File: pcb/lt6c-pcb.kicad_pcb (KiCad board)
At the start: 2 copper layers, 62 x 66.4 mm, 19 parts, among them SW1 SW_Push, SW2 SW_Push, SW3 SW_Push, SW4 SW_Push, SW5 SW_Push, SW6 SW_Push, U1 XIAO-RP2040, U2 TPS76318, U3 PMW3360DM-T2QU

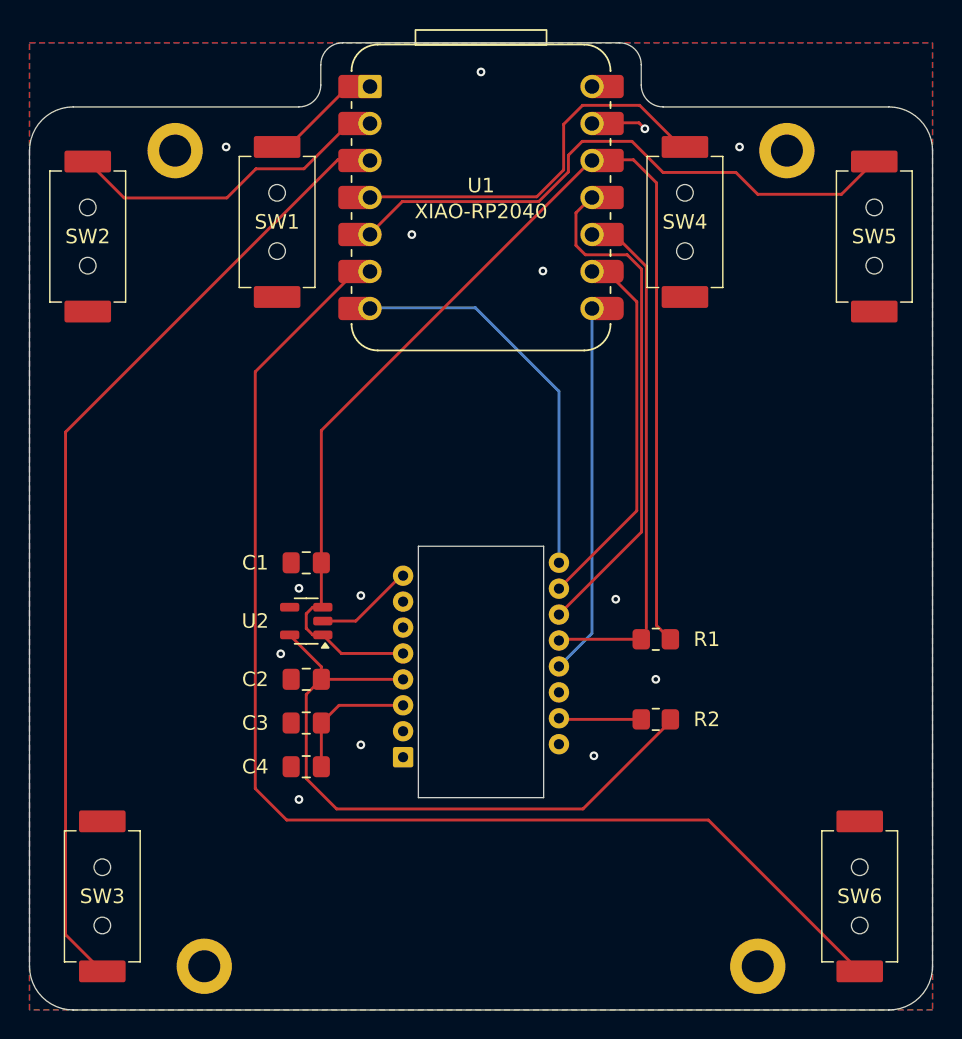
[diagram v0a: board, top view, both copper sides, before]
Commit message: Add silkscreen pattern and infos
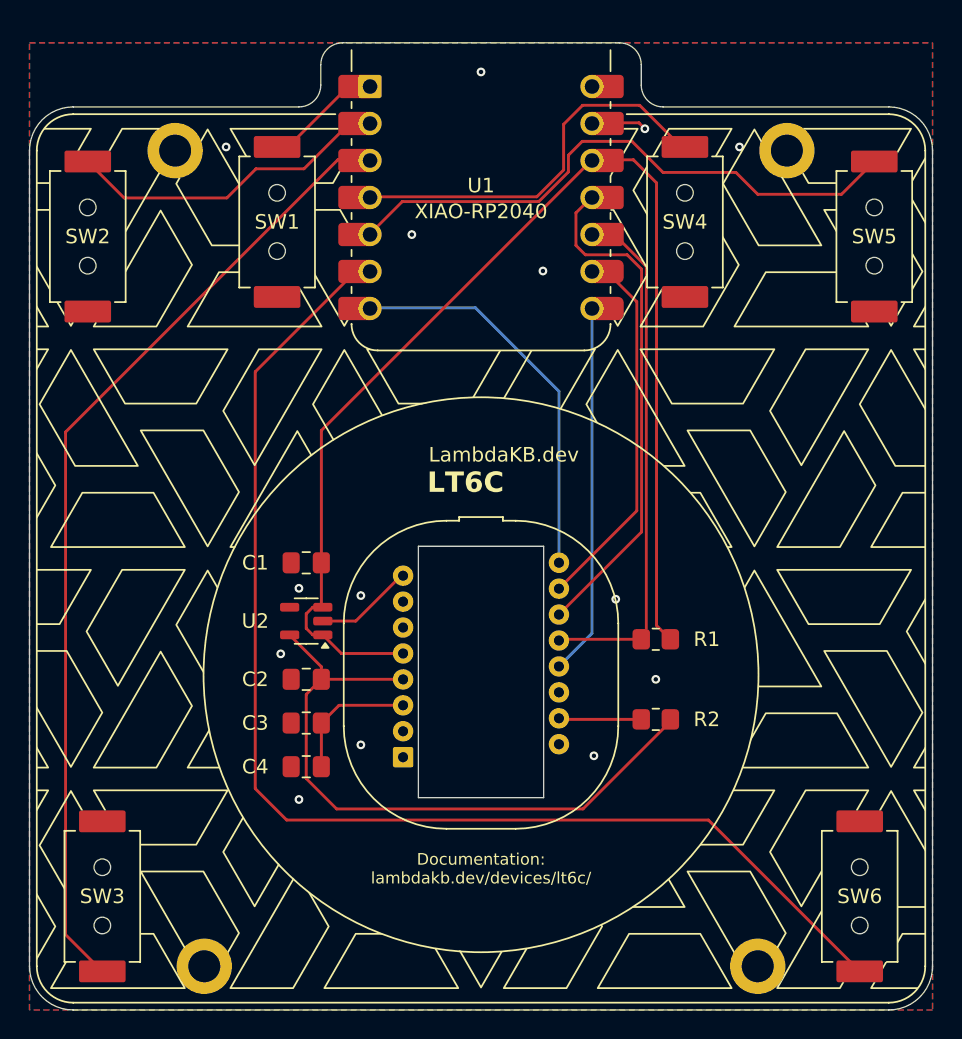
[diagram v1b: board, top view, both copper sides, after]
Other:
- board text added: "2025 - LambdaKB.dev"
- board text added: "CERN-OHL-S-2.0"
- board text added: "Documentation: lambdakb.dev/devices/lt6c/"
- board text added: "LT6C"
- board text added: "LT6C v1.00"
- board text added: "LambdaKB.dev"
- board text added: "PMW3360DM"

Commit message: Update README.md & .gitattributes
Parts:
- H1, H2, H3, H4: value MountingHole_M2 -> MountingHole_Pad
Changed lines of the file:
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@@
 			)
 		)
-		(property "Value" "MountingHole_M2"
+		(property "Value" "MountingHole_Pad"
 			(at 0 2.9 0)
 			(layer "F.Fab")
@@
 			)
 		)
-		(property "Value" "MountingHole_M2"
+		(property "Value" "MountingHole_Pad"
 			(at 0 2.9 0)
 			(layer "F.Fab")
@@
 			)
 		)
-		(property "Value" "MountingHole_M2"
+		(property "Value" "MountingHole_Pad"
 			(at 0 2.9 0)
 			(layer "F.Fab")
@@
 			)
 		)
-		(property "Value" "MountingHole_M2"
+		(property "Value" "MountingHole_Pad"
 			(at 0 2.9 0)
 			(layer "F.Fab")
@@
 			)
 		)
-		(property "Datasheet" ""
+		(property "Datasheet" "https://www.epsglobal.com/Media-Library/EPSGlobal/Products/files/pixart/PMW3360DM-T2QU.pdf"
 			(at 0 0 180)
 			(layer "B.Fab")

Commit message: Update silkscreen
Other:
- board text added: "Licensed under"

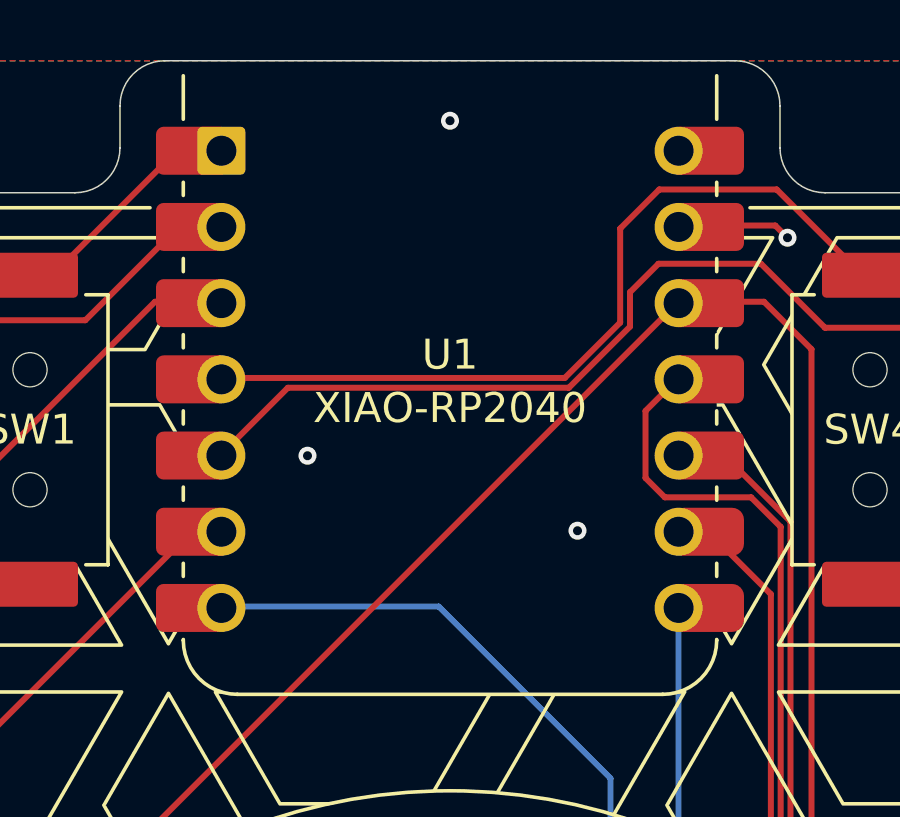
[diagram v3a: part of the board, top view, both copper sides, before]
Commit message: Add pinouts to XIAO-RP2040 and cleanup silkscreen
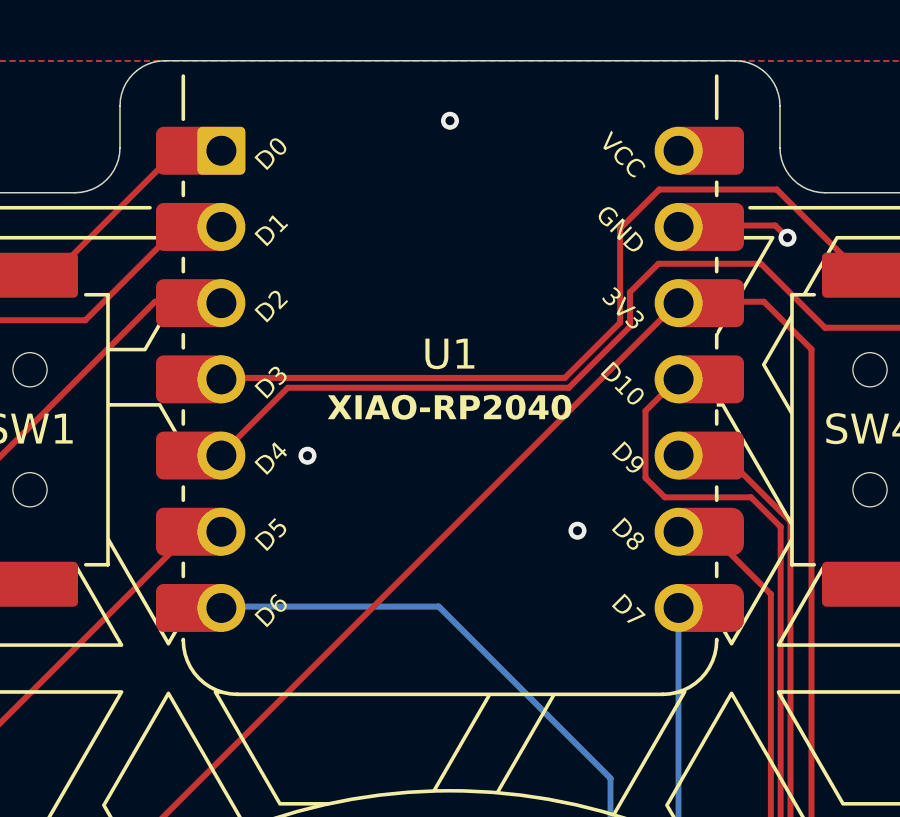
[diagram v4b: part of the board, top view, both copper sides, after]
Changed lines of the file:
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@@
 	(net 27 "unconnected-(U3-NC-Pad14)")
 	(net 28 "unconnected-(U3-NC-Pad6)")
-	(net 29 "unconnected-(U1-5V-Pad14)")
 	(footprint "Capacitor_SMD:C_0805_2012Metric_Pad1.18x1.45mm_HandSolder"
 		(layer "F.Cu")
@@
 			(effects
 				(font
-					(size 1 1)
-					(thickness 0.15)
+					(size 0.8 0.8)
+					(thickness 0.16)
+					(bold yes)
 				)
 			)
@@
 		(fp_line
 			(start -8.89 -1.05)
-			(end -8.89 -2.5)
+			(end -8.89 -2.4892)
 			(stroke
 				(width 0.12)
@@
 		)
 		(fp_line
-			(start 8.89 -1.05)
-			(end 8.89 -2.5)
+			(start 8.89 -2.4892)
+			(end 8.89 -1.08)
 			(stroke
 				(width 0.12)
@@
 			(layer "F.Fab")
 		)
-		(fp_rect
-			(start -4.5 -2.88)
-			(end 4.5 -3.88)
-			(stroke
-				(width 0.12)
-				(type solid)
+		(fp_text user "D8"
+			(at 6.35 13.208 -45)
+			(unlocked yes)
+			(layer "F.SilkS")
+			(effects
+				(font
+					(size 0.6 0.6)
+					(thickness 0.12)
+				)
+				(justify right)
+			)
+		)
+		(fp_text user "D1"
+			(at -6.35 3.048 45)
+			(unlocked yes)
+			(layer "F.SilkS")
+			(effects
+				(font
+					(size 0.6 0.6)
+					(thickness 0.12)
+				)
+				(justify left)
+			)
+		)
+		(fp_text user "D10"
+			(at 6.35 8.382 -45)
+			(unlocked yes)
+			(layer "F.SilkS")
+			(effects
+				(font
+					(size 0.6 0.6)
+					(thickness 0.12)
+				)
+				(justify right)
+			)
+		)
+		(fp_text user "D0"
+			(at -6.35 0.508 45)
+			(unlocked yes)
+			(layer "F.SilkS")
+			(effects
+				(font
+					(size 0.6 0.6)
+					(thickness 0.12)
+				)
+				(justify left)
+			)
+		)
+		(fp_text user "VCC"
+			(at 6.35 0.762 -45)
+			(unlocked yes)
+			(layer "F.SilkS")
+			(effects
+				(font
+					(size 0.6 0.6)
+					(thickness 0.12)
+				)
+				(justify right)
+			)
+		)
+		(fp_text user "D4"
+			(at -6.35 10.668 45)
+			(unlocked yes)
+			(layer "F.SilkS")
+			(effects
+				(font
+					(size 0.6 0.6)
+					(thickness 0.12)
+				)
+				(justify left)
+			)
+		)
+		(fp_text user "3V3"
+			(at 6.35 5.842 -45)
+			(unlocked yes)
+			(layer "F.SilkS")
+			(effects
+				(font
+					(size 0.6 0.6)
+					(thickness 0.12)
+				)
+				(justify right)
+			)
+		)
+		(fp_text user "D6"
+			(at -6.35 15.748 45)
+			(unlocked yes)
+			(layer "F.SilkS")
+			(effects
+				(font
+					(size 0.6 0.6)
+					(thickness 0.12)
+				)
+				(justify left)
+			)
+		)
+		(fp_text user "D3"
+			(at -6.35 8.128 45)
+			(unlocked yes)
+			(layer "F.SilkS")
+			(effects
+				(font
+					(size 0.6 0.6)
+					(thickness 0.12)
+				)
+				(justify left)
+			)
+		)
+		(fp_text user "GND"
+			(at 6.35 3.302 -45)
+			(unlocked yes)
+			(layer "F.SilkS")
+			(effects
+				(font
+					(size 0.6 0.6)
+					(thickness 0.12)
+				)
+				(justify right)
+			)
+		)
+		(fp_text user "D9"
+			(at 6.35 10.668 -45)
+			(unlocked yes)
+			(layer "F.SilkS")
+			(effects
+				(font
+					(size 0.6 0.6)
+					(thickness 0.12)
+				)
+				(justify right)
+			)
+		)
+		(fp_text user "D5"
+			(at -6.35 13.208 45)
+			(unlocked yes)
+			(layer "F.SilkS")
+			(effects
+				(font
+					(size 0.6 0.6)
+					(thickness 0.12)
+				)
+				(justify left)
+			)
+		)
+		(fp_text user "D2"
+			(at -6.35 5.588 45)
+			(unlocked yes)
+			(layer "F.SilkS")
+			(effects
+				(font
+					(size 0.6 0.6)
+					(thickness 0.12)
+				)
+				(justify left)
+			)
+		)
+		(fp_text user "D7"
+			(at 6.35 15.748 -45)
+			(unlocked yes)
+			(layer "F.SilkS")
+			(effects
+				(font
+					(size 0.6 0.6)
+					(thickness 0.12)
+				)
+				(justify right)
 			)
-			(fill none)
-			(layer "F.Fab")
 		)
 		(fp_text user "${REFERENCE}"
@@
 			(layers "F.Cu" "F.Paste" "F.Mask")
 			(roundrect_rratio 0.16)
-			(net 29 "unconnected-(U1-5V-Pad14)")
+			(net 22 "unconnected-(U1-5V-Pad14)_1")
 			(pinfunction "5V")
 			(pintype "power_in+no_connect")

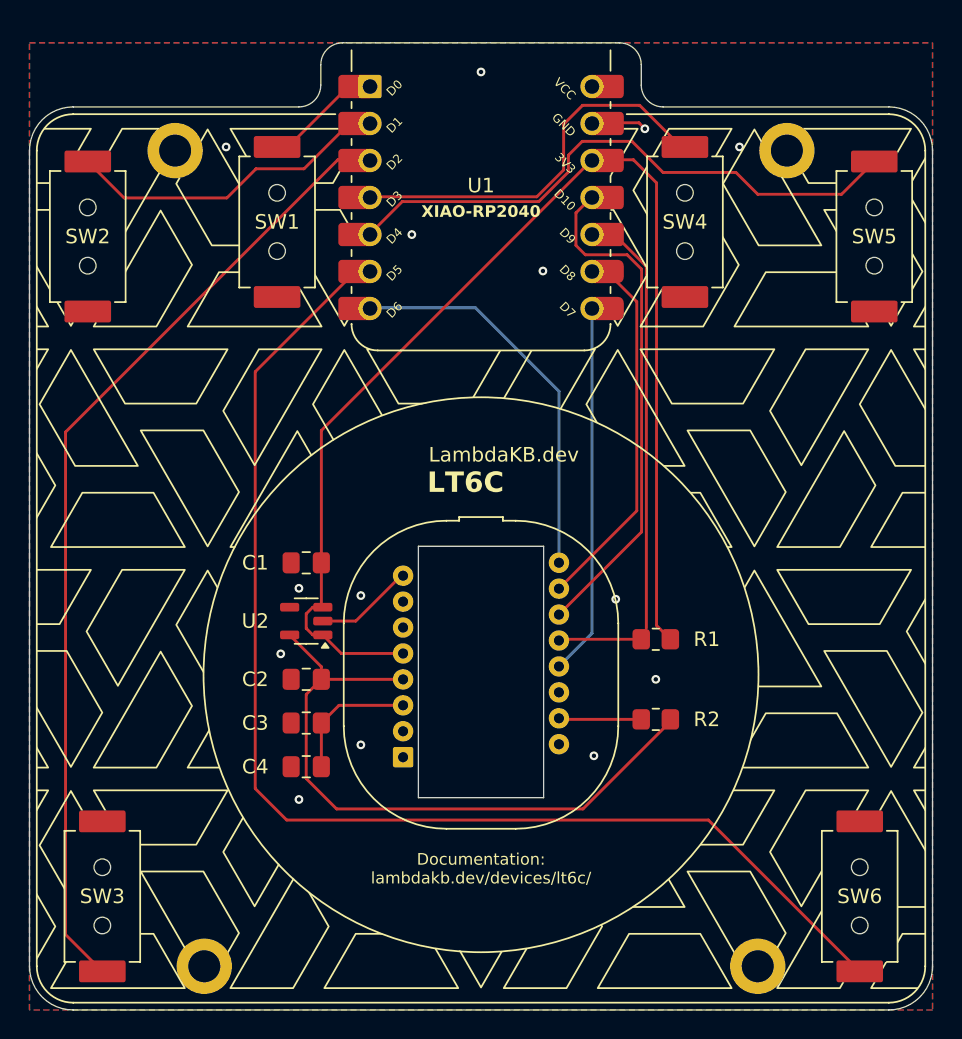
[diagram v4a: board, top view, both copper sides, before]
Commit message: Fix ERC/DRC + update LKBD libraries
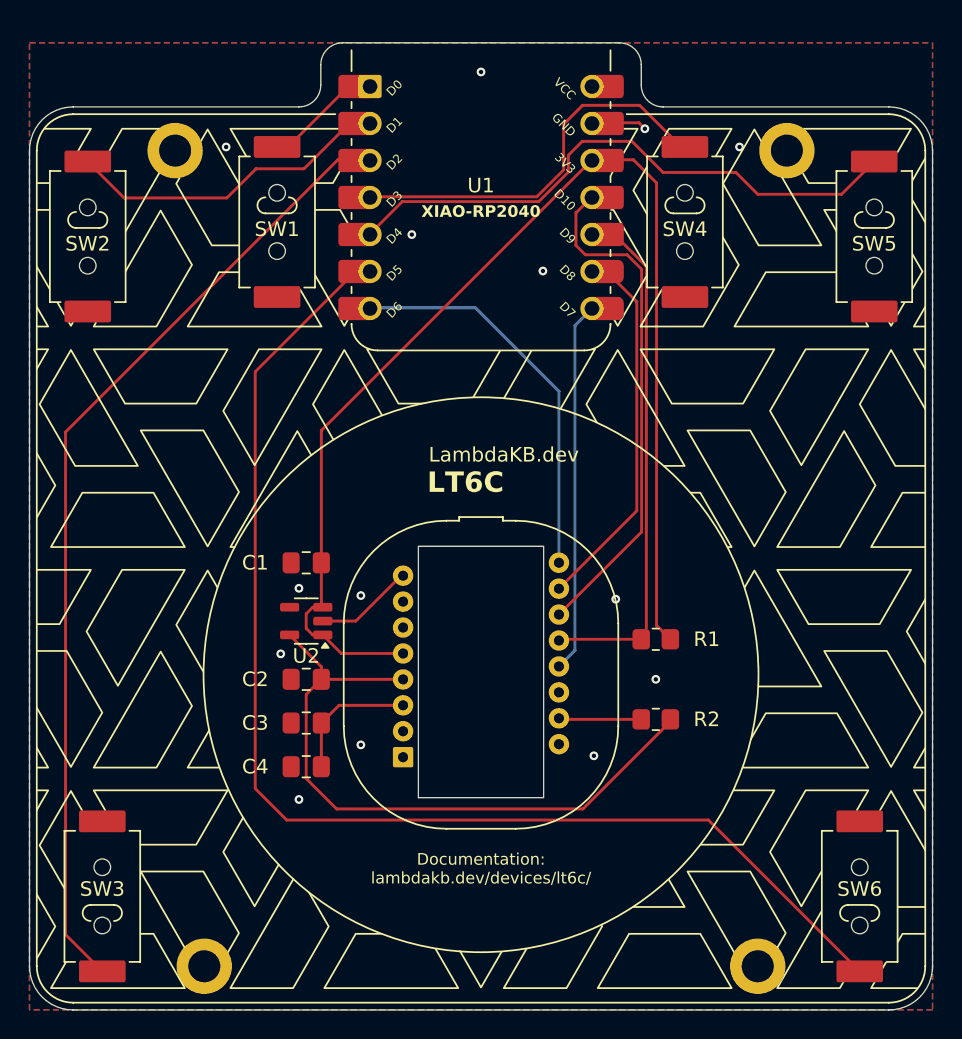
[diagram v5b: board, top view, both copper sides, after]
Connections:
- U3 pad 7: /NRESET -> unconnected-(U3-~{RESET}-Pad7)
